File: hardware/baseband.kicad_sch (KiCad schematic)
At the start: 32 parts, among them U6 MCP6002, U7 MCP6002

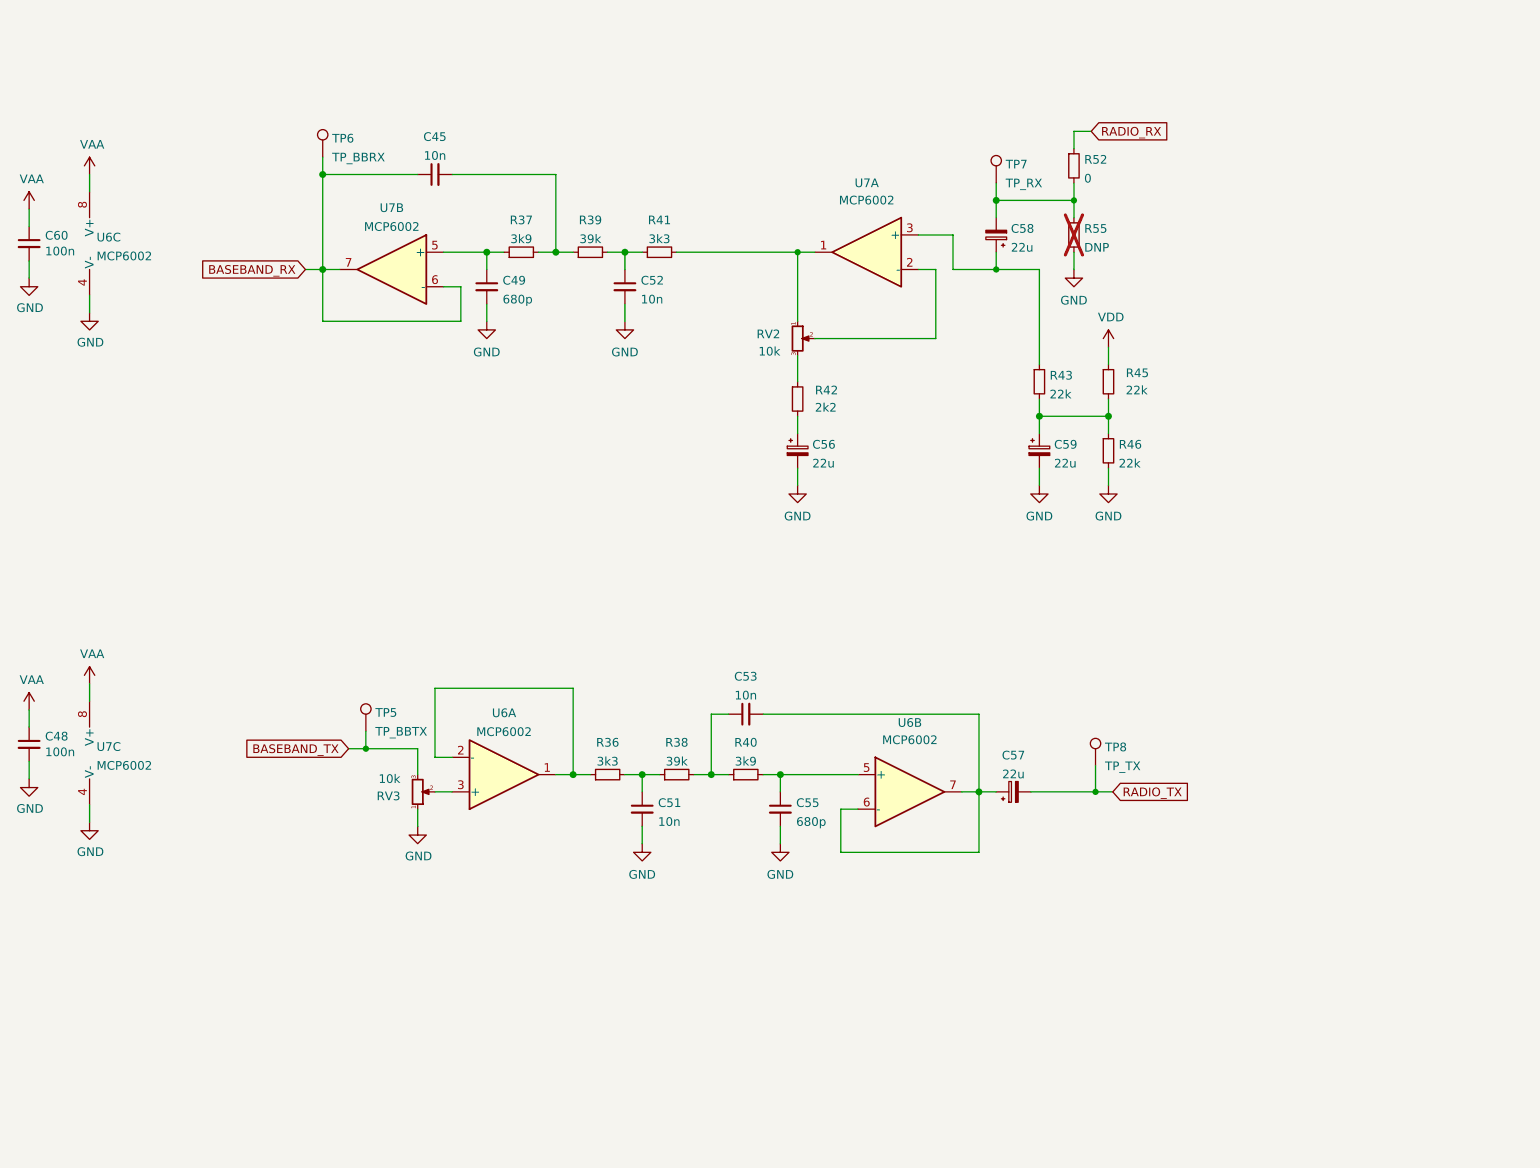
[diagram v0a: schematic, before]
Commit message: Placed both e-potentiometers and multiturn potentiometers on schematic
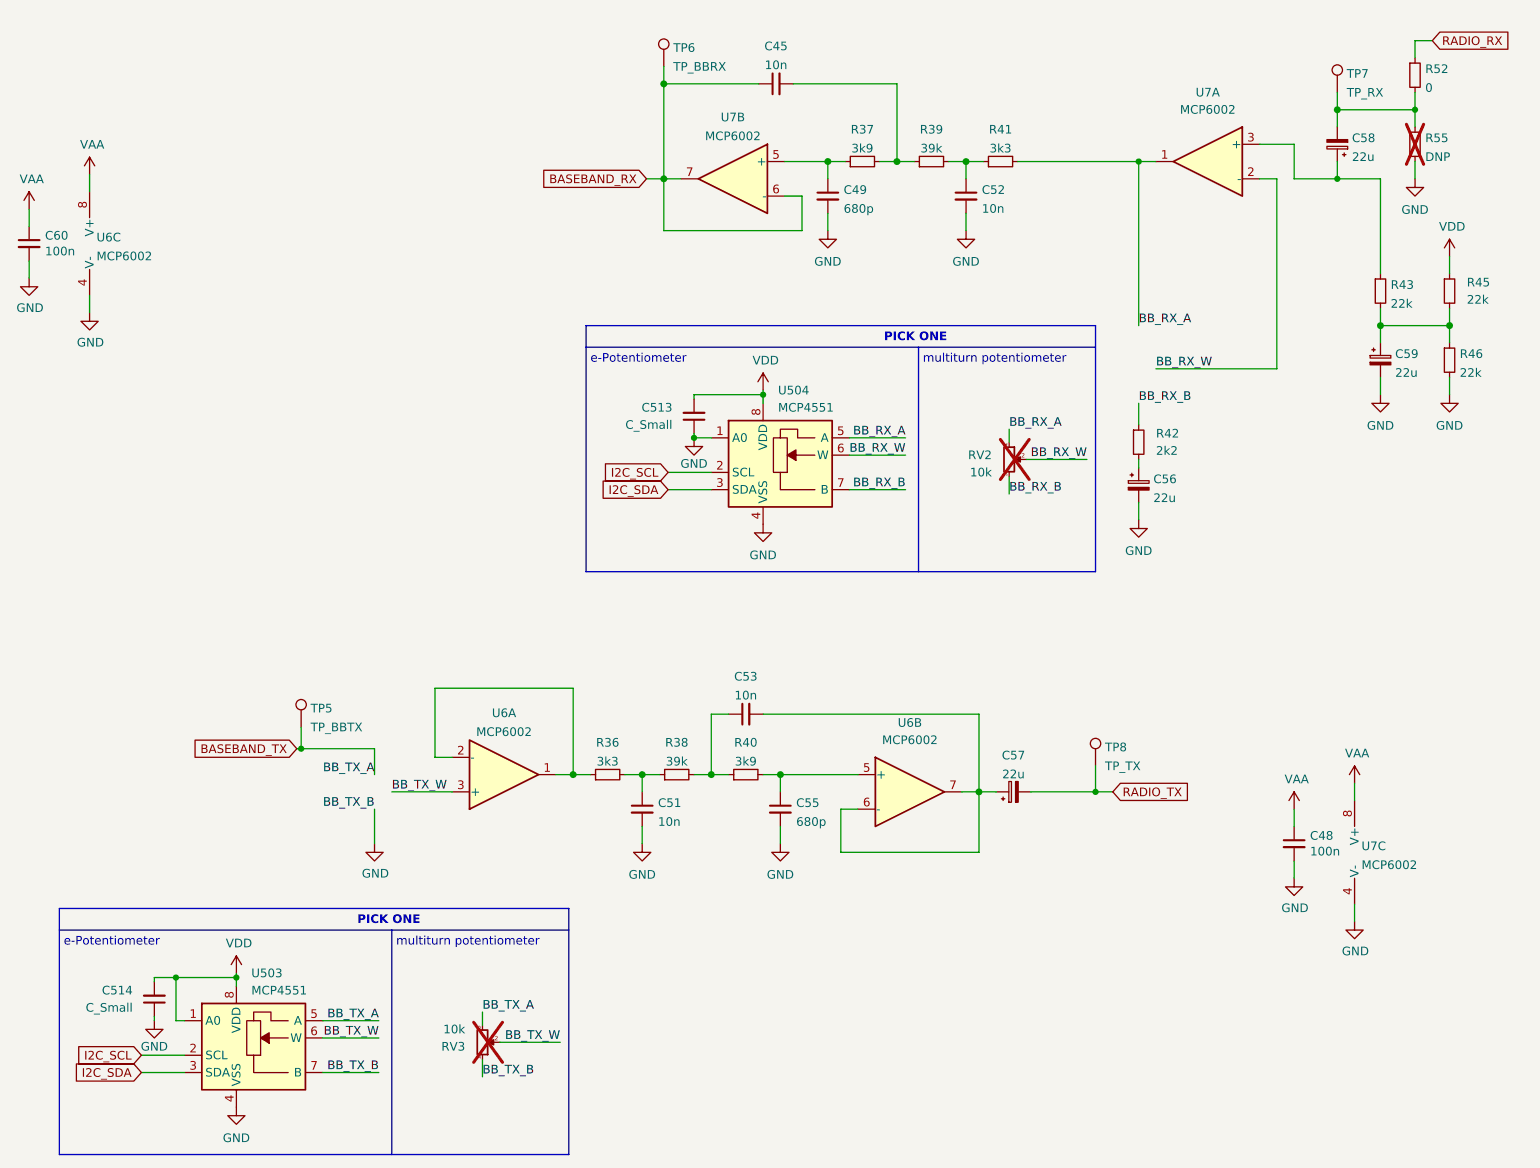
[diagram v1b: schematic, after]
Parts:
- added C513, C514: C_Small, symbol Device:C_Small
- added U503, U504: MCP4551, Package_SO:MSOP-8_3x3mm_P0.65mm, symbol Module17:MCP4551
- RV2, RV3: now not fitted
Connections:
- net BASEBAND_TX: now also U503.5 (A)
- net GND: now also C513.1, C514.1, U503.4 (VSS), U503.7 (B), U504.1 (A0), U504.4 (VSS)
- net VDD: now also C513.2, C514.2, U503.1 (A0), U503.8 (VDD), U504.8 (VDD)
- net BB_TX_W: now reaches RV3.2, U6.3 (+)
- net BB_TX_W: now also U503.6 (W)
- net BB_RX_A: now reaches R41.2, RV2.1, U7.1
- net BB_RX_A: now also U504.5 (A)
- net BB_RX_B: now reaches R42.1, RV2.3
- net BB_RX_B: now also U504.7 (B)
- net BB_RX_W: now reaches RV2.2, U7.2 (-)
- net BB_RX_W: now also U504.6 (W)
- new net I2C_SCL: U503.2 (SCL), U504.2 (SCL)
- new net I2C_SDA: U503.3 (SDA), U504.3 (SDA)
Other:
- note added: "PICK ONE"
- note added: "e-Potentiometer"
- note added: "multiturn potentiometer"
- moved on the sheet: C45, C48, C49, C52, C56, C58, C59, R37, R39, R41, R42, R43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

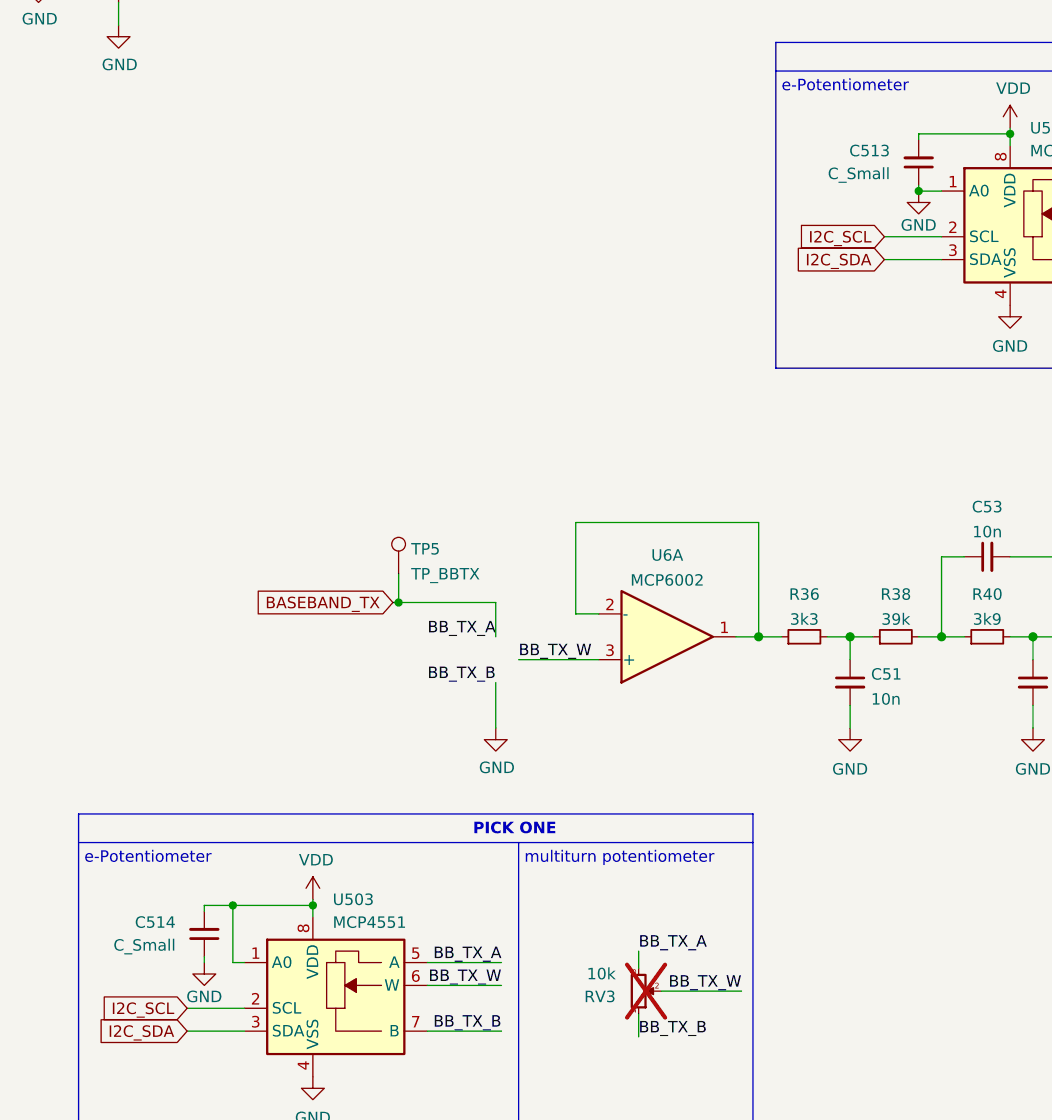
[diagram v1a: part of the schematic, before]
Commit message: Assigned footprints
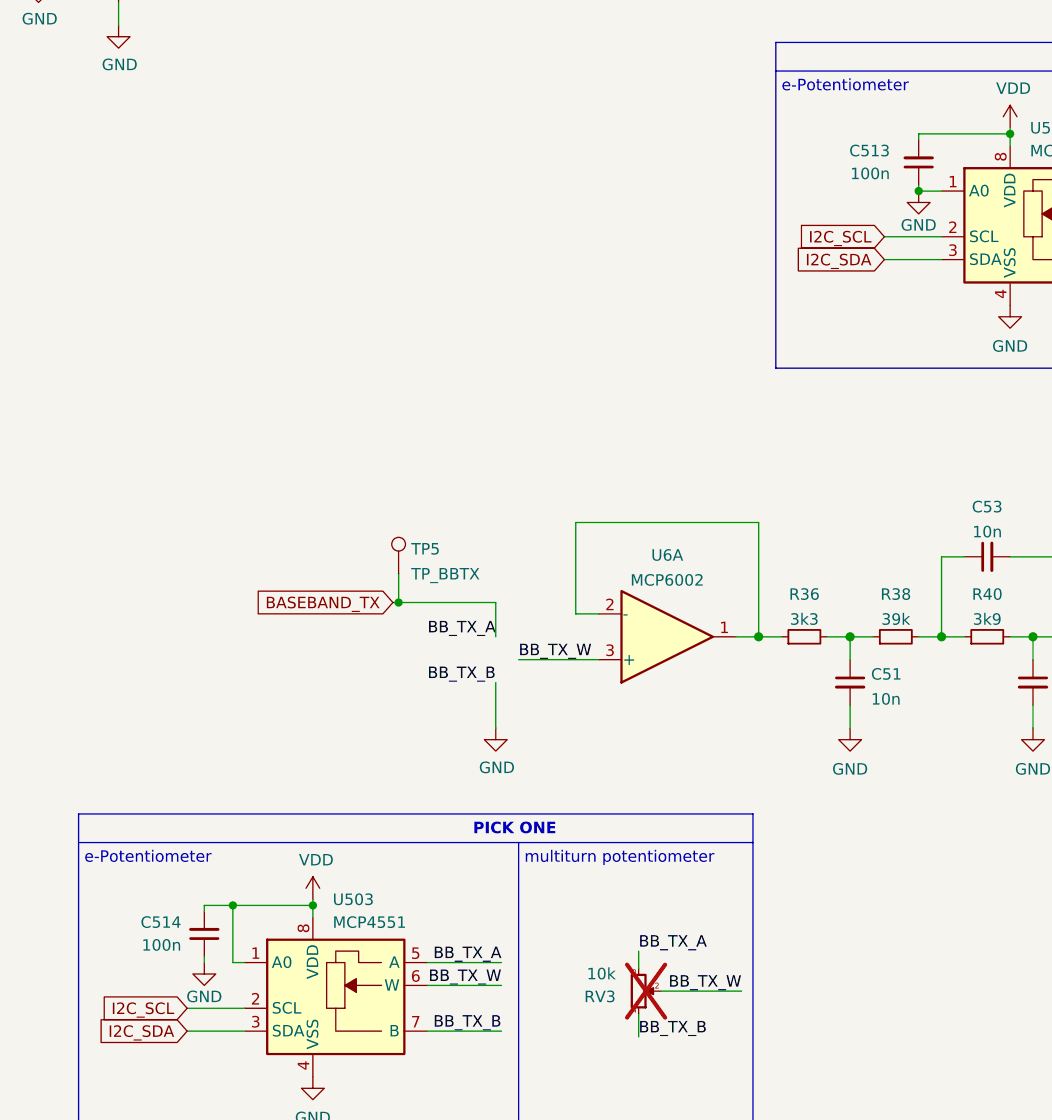
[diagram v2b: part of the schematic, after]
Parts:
- C513, C514: value C_Small -> 100n; footprint (none) -> pkl_dipol:C_0603
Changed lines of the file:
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@@
   (symbol (lib_id "Device:C_Small") (at 50.8 164.465 0) (mirror x) (unit 1)
     (in_bom yes) (on_board yes) (dnp no) (fields_autoplaced)
-    (property "Reference" "C514" (at 47.625 163.1886 0)
+    (property "Reference" "C514" (at 48.26 163.1886 0)
       (effects (font (size 1.27 1.27)) (justify right))
     )
-    (property "Value" "C_Small" (at 47.625 165.7286 0)
+    (property "Value" "100n" (at 48.26 165.7286 0)
       (effects (font (size 1.27 1.27)) (justify right))
     )
-    (property "Footprint" "" (at 50.8 164.465 0)
+    (property "Footprint" "pkl_dipol:C_0603" (at 50.8 164.465 0)
       (effects (font (size 1.27 1.27)) hide)
     )
@@
       (effects (font (size 1.27 1.27)) (justify right))
     )
-    (property "Value" "C_Small" (at 127 80.0036 0)
+    (property "Value" "100n" (at 127 80.0036 0)
       (effects (font (size 1.27 1.27)) (justify right))
     )
-    (property "Footprint" "" (at 130.175 78.74 0)
-      (effects (font (size 1.27 1.27)) hide)
-    )
+    (property "Footprint" "pkl_dipol:C_0603" (at 130.175 78.74 0)
+      (effects (font (size 1.27 1.27)) hide)
+    )

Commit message: Started new PCB layout
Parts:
- RV2, RV3: footprint Potentiometer_SMD:Potentiometer_Bourns_3224W_Vertical -> Potentiometer_SMD:Potentiometer_Bourns_3224J_Horizontal
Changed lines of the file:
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@@
       (effects (font (size 1.27 1.27)) (justify right))
     )
-    (property "Footprint" "Potentiometer_SMD:Potentiometer_Bourns_3224W_Vertical" (at 176.53 85.09 0)
+    (property "Footprint" "Potentiometer_SMD:Potentiometer_Bourns_3224J_Horizontal" (at 176.53 85.09 0)
       (effects (font (size 1.27 1.27)) hide)
     )
@@
       (effects (font (size 1.27 1.27)) (justify right))
     )
-    (property "Footprint" "Potentiometer_SMD:Potentiometer_Bourns_3224W_Vertical" (at 99.06 170.815 0)
-      (effects (font (size 1.27 1.27)) hide)
-    )
+    (property "Footprint" "Potentiometer_SMD:Potentiometer_Bourns_3224J_Horizontal" (at 99.06 170.815 0)
+      (effects (font (size 1.27 1.27)) hide)
+    )
